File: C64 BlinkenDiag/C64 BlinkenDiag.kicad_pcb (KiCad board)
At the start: 2 copper layers, 99.4 x 99.9 mm, 13 parts, among them J1 C64-Exp-Port, J2 Voltmeter, M1 Mounting, M2 Mounting, M3 Mounting, M4 Mounting, SW1 ROM_EN, SW2 Function, SW3 Bank, SW4 Reset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

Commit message: Did a layout
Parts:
- added A1: module, voltmeter:voltage_display_036, F.Cu at (191.4, 28.6)
- added C1: 100nF, Capacitor_THT:C_Disc_D4.7mm_W2.5mm_P5.00mm, F.Cu at (135.5, 87.0)
- added C2: 100nF, Capacitor_THT:C_Disc_D4.7mm_W2.5mm_P5.00mm, F.Cu at (132.3, 37.5)
- added C3: 100nF, Capacitor_THT:C_Disc_D4.7mm_W2.5mm_P5.00mm, F.Cu at (146.3, 37.5)
- added C4: 100nF, Capacitor_THT:C_Disc_D4.7mm_W2.5mm_P5.00mm, F.Cu at (169.8, 74.3)
- added C5: 100nF, Capacitor_THT:C_Disc_D4.7mm_W2.5mm_P5.00mm, F.Cu at (138.0, 74.3)
- added C6: 10uF, Capacitor_THT:CP_Radial_D4.0mm_P2.00mm, F.Cu at (124.1, 82.5)
- added D1: RESET, LED_THT:LED_D5.0mm, F.Cu at (169.2, 26.0)
- added D10: D6, LED_THT:LED_D5.0mm, F.Cu at (161.5, 41.3)
- added D11: D5, LED_THT:LED_D5.0mm, F.Cu at (168.5, 41.3)
- added D12: D4, LED_THT:LED_D5.0mm, F.Cu at (175.5, 41.3)
- added D13: D3, LED_THT:LED_D5.0mm, F.Cu at (183.1, 41.3)
- added D14: D2, LED_THT:LED_D5.0mm, F.Cu at (190.1, 41.3)
- added D15: D1, LED_THT:LED_D5.0mm, F.Cu at (197.1, 41.3)
- added D16: D0, LED_THT:LED_D5.0mm, F.Cu at (204.1, 41.3)
- added D17: A15, LED_THT:LED_D5.0mm, F.Cu at (154.6, 52.7)
- added D18: A14, LED_THT:LED_D5.0mm, F.Cu at (161.5, 52.7)
- added D19: A13, LED_THT:LED_D5.0mm, F.Cu at (168.5, 52.7)
- added D2: GAME, LED_THT:LED_D5.0mm, F.Cu at (131.7, 26.0)
- added D20: A12, LED_THT:LED_D5.0mm, F.Cu at (175.5, 52.7)
- added D21: A11, LED_THT:LED_D5.0mm, F.Cu at (183.1, 52.7)
- added D22: A10, LED_THT:LED_D5.0mm, F.Cu at (190.1, 52.7)
- added D23: A9, LED_THT:LED_D5.0mm, F.Cu at (197.1, 52.7)
- added D24: A8, LED_THT:LED_D5.0mm, F.Cu at (204.1, 52.7)
- added D25: A7, LED_THT:LED_D5.0mm, F.Cu at (154.6, 64.1)
- added D26: A6, LED_THT:LED_D5.0mm, F.Cu at (161.5, 64.1)
- added D27: A5, LED_THT:LED_D5.0mm, F.Cu at (168.5, 64.1)
- added D28: A4, LED_THT:LED_D5.0mm, F.Cu at (175.5, 64.1)
- added D29: A3, LED_THT:LED_D5.0mm, F.Cu at (183.1, 64.1)
- added D3: EXROM, LED_THT:LED_D5.0mm, F.Cu at (138.7, 26.0)
- added D30: A2, LED_THT:LED_D5.0mm, F.Cu at (190.1, 64.1)
- added D31: A1, LED_THT:LED_D5.0mm, F.Cu at (197.1, 64.1)
- added D32: A0, LED_THT:LED_D5.0mm, F.Cu at (204.1, 64.1)
- added D4: IO2, LED_THT:LED_D5.0mm, F.Cu at (145.7, 26.0)
- added D5: IO1, LED_THT:LED_D5.0mm, F.Cu at (152.7, 26.0)
- added D6: WRITE, LED_THT:LED_D5.0mm, F.Cu at (162.2, 26.0)
- added D7: IRQ, LED_THT:LED_D5.0mm, F.Cu at (162.2, 33.0)
- added D8: NMI, LED_THT:LED_D5.0mm, F.Cu at (169.2, 33.0)
- added D9: D7, LED_THT:LED_D5.0mm, F.Cu at (154.6, 41.3)
- added JP1: EN_SIGNAL, Connector_PinHeader_2.54mm:PinHeader_1x03_P2.54mm_Vertical, F.Cu at (124.7, 70.5)
- added JP2: EN_DATA, Connector_PinHeader_2.54mm:PinHeader_1x03_P2.54mm_Vertical, F.Cu at (127.3, 70.5)
- added JP3: EN_ADDR, Connector_PinHeader_2.54mm:PinHeader_1x03_P2.54mm_Vertical, F.Cu at (132.3, 70.5)
- added JP4: EN_ADDR, Connector_PinHeader_2.54mm:PinHeader_1x03_P2.54mm_Vertical, F.Cu at (134.9, 70.5)
- added RN1: 330x8, Resistor_THT:R_Array_SIP9, F.Cu at (157.1, 45.7)
- added RN2: 330x8, Resistor_THT:R_Array_SIP9, F.Cu at (131.7, 32.4)
- added RN3: 330x8, Resistor_THT:R_Array_SIP9, F.Cu at (157.1, 57.1)
- added RN4: 330x8, Resistor_THT:R_Array_SIP9, F.Cu at (157.1, 68.6)
- added U2: 74HCT540, Package_DIP:DIP-20_W7.62mm_Socket_LongPads, F.Cu at (124.7, 41.3)
- added U3: 74HCT573, Package_DIP:DIP-20_W7.62mm_Socket_LongPads, F.Cu at (138.7, 41.3)
- added U4: 74HCT573, Package_DIP:DIP-20_W7.62mm_Socket_LongPads, F.Cu at (173.6, 81.9)
- added U5: 74HCT573, Package_DIP:DIP-20_W7.62mm_Socket_LongPads, F.Cu at (141.9, 81.9)
- M1, M2, M3, M4: footprint mounting:M3 -> mounting:M3_pin
- SW2: value Function -> FUNCTION
- SW3: value Bank -> ROM_BANK
- SW4: value Reset -> RESET
- moved SW2 213.0 mm to (214.2, 54.0)
- moved J2 204.2 mm to (215.5, 33.0), turned to 180 degrees
- moved SW1 202.6 mm to (214.2, 76.8)
- moved SW3 198.0 mm to (214.2, 65.4)
- moved R2 121.0 mm to (125.1, 99.1)
- moved R1 113.0 mm to (125.1, 95.9)
- moved SW4 36.6 mm to (214.2, 41.9)
- moved U1 2.29 mm to (139.3, 102.2)
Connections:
- net A13 renamed ROM_A13
- net A14 renamed ROM_A14
- net ~ROM renamed ~ROM_CS
- J1 pad 10: (no net) -> /~IO2
- J1 pad 4: (no net) -> /~IRQ
- J1 pad 5: (no net) -> /R~W
- J1 pad 7: (no net) -> /~IO1
- J1 pad D: (no net) -> /~NMI
- J1 pad E: (no net) -> /PHI2
- J1 pad F: Net-(J1-PadF) -> /A15
- J1 pad H: Net-(J1-PadH) -> /A14
- J1 pad J: Net-(J1-PadJ) -> /A13
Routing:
- net VCC: track 0.00 -> 273.5 mm, vias 0 -> 4
- net ~RESET: track 0.00 -> 212.4 mm, vias 0 -> 1
- net ~GAME: track 0.00 -> 171.6 mm, vias 0 -> 8
- net ~EXROM: track 0.00 -> 161.5 mm, vias 0 -> 4
- net ~ROMH: track 0.00 -> 146.5 mm, vias 0 -> 7
- net /PHI2: track 0.00 -> 135.9 mm, vias 0 -> 3
- net ROM_A13: track 0.00 -> 130.9 mm, vias 0 -> 3
- net ~ROML: track 0.00 -> 128.5 mm, vias 0 -> 4
- net Net-(D18-Pad2): track 0.00 -> 110.3 mm
- net /D6: track 0.00 -> 98.2 mm, vias 0 -> 1
- net Net-(D19-Pad2): track 0.00 -> 97.8 mm
- net ~ROM_CS: track 8.15 -> 105.6 mm, vias 0 -> 2
- net Net-(D17-Pad2): track 0.00 -> 97.0 mm, vias 0 -> 2
- net ROM_A14: track 0.00 -> 96.1 mm, vias 0 -> 4
- net /D7: track 0.00 -> 95.1 mm, vias 0 -> 1
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- added copper zone on F.Cu, net VCC
- removed copper zone on F.Cu, net +5V

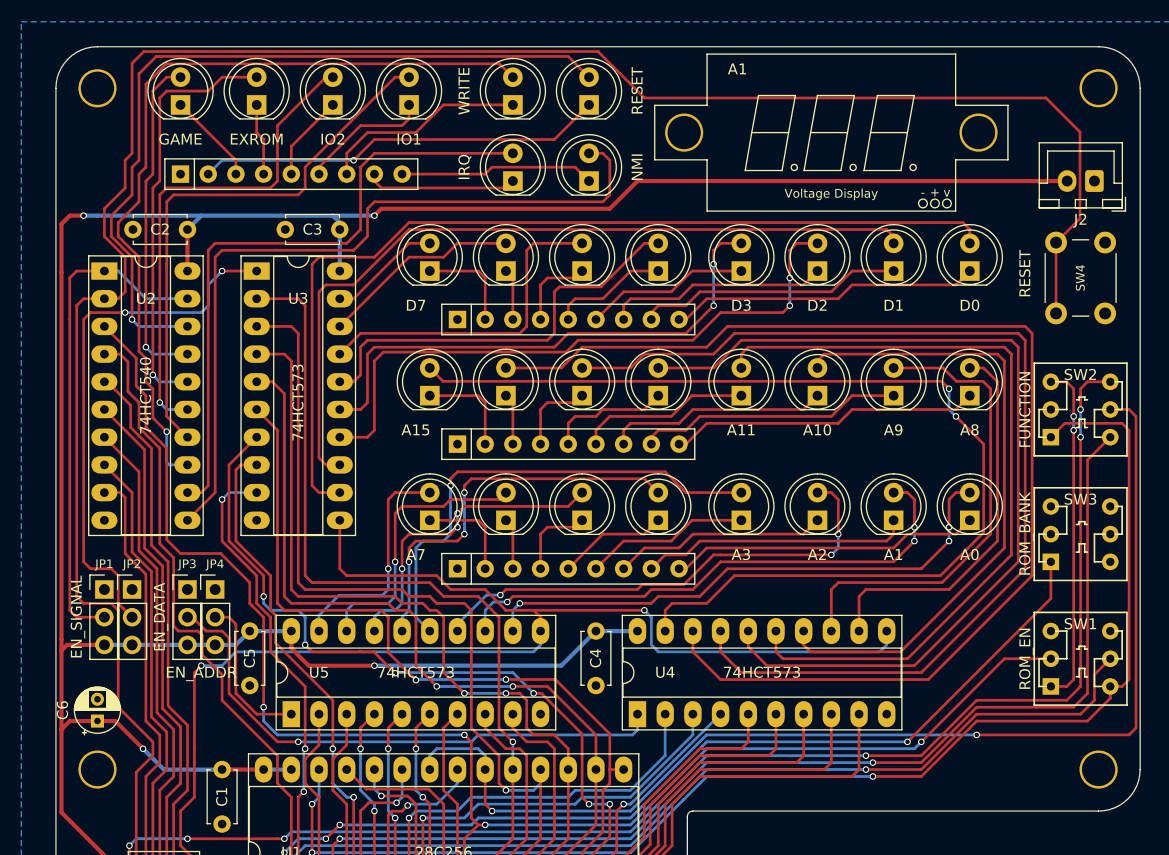
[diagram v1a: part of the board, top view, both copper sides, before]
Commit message: Tweaked silkscreen and gerber export
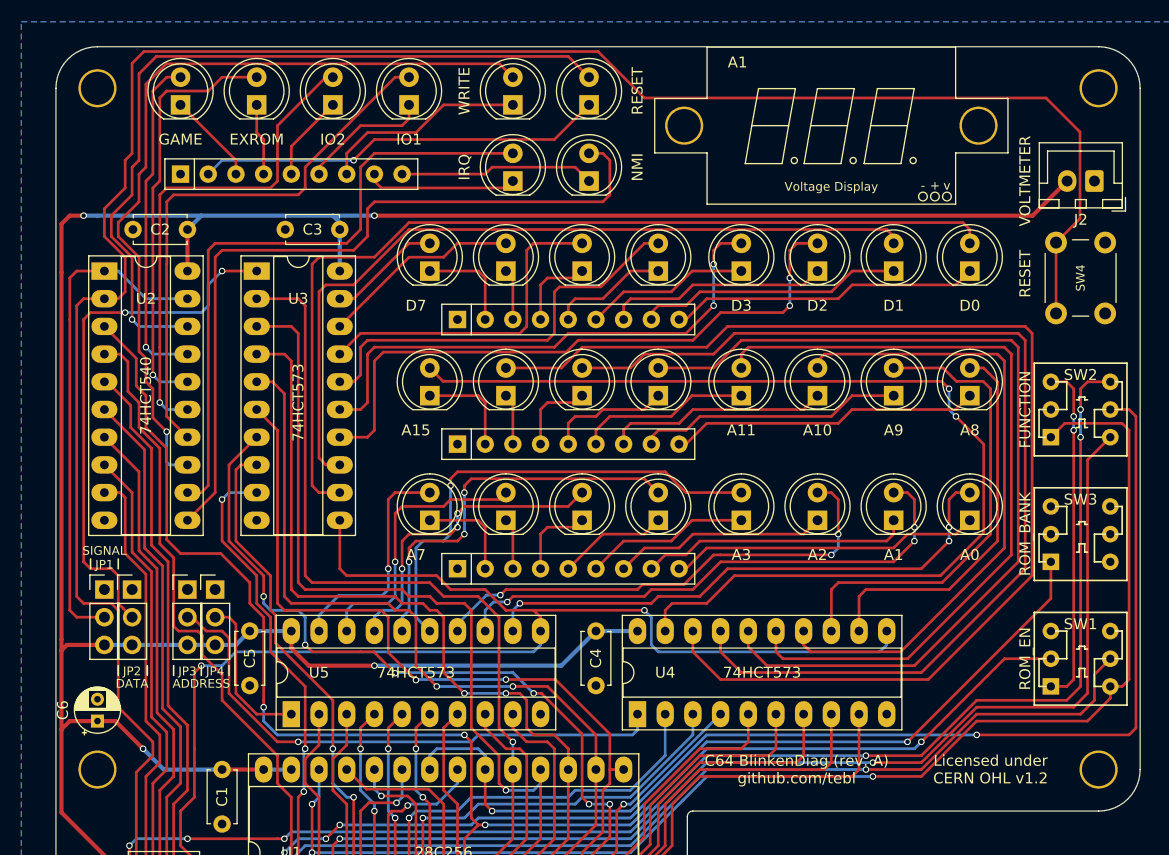
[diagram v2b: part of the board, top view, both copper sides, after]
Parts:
- J2: value Voltmeter -> VOLTMETER
- moved A1 0.63 mm to (191.4, 27.9)
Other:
- board text added: "ADDRESS"
- board text added: "C64 BlinkenDiag (rev. A) github.com/tebl"
- board text added: "DATA"
- board text added: "GND"
- board text added: "LED Output: 1-2 Enabled 2-3 Disabled"
- board text added: "Licensed under CERN OHL v1.2"
- board text added: "SIGNAL"
- board text added: "VCC"

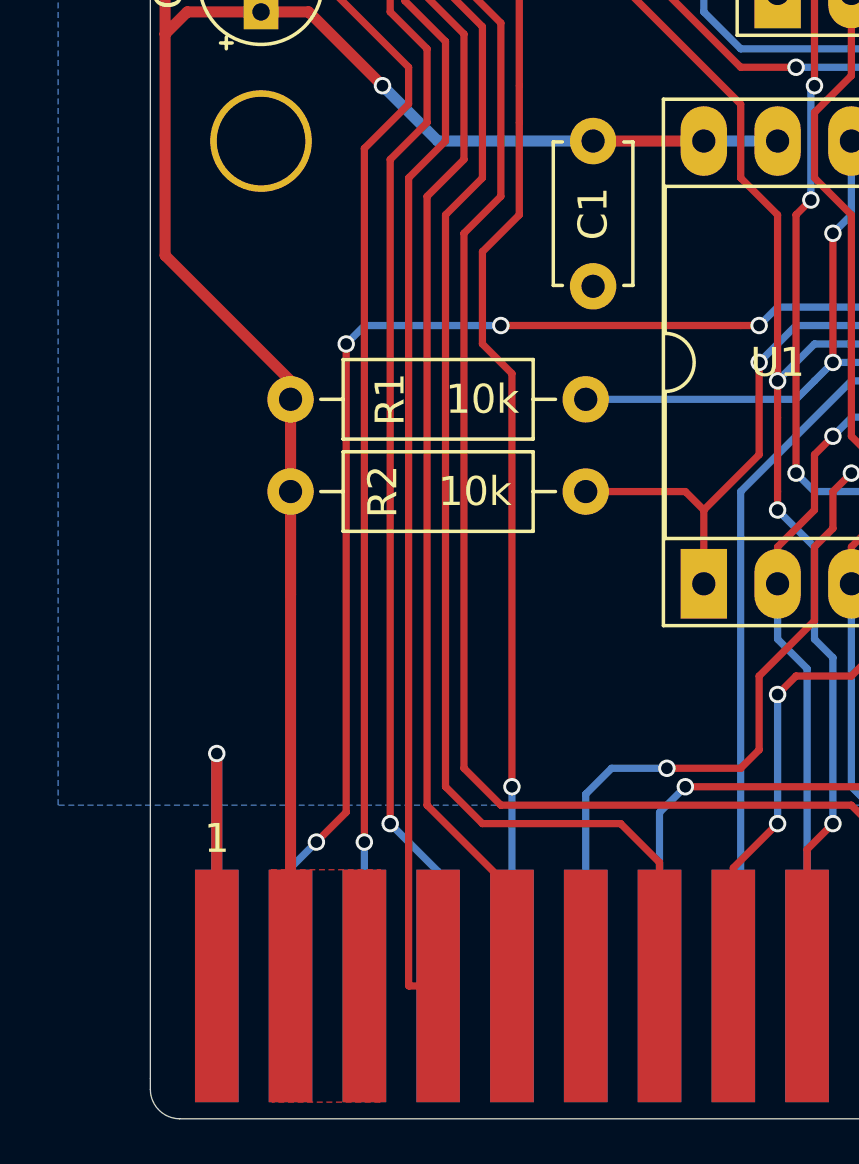
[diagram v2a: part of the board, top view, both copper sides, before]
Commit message: Add PCB preview
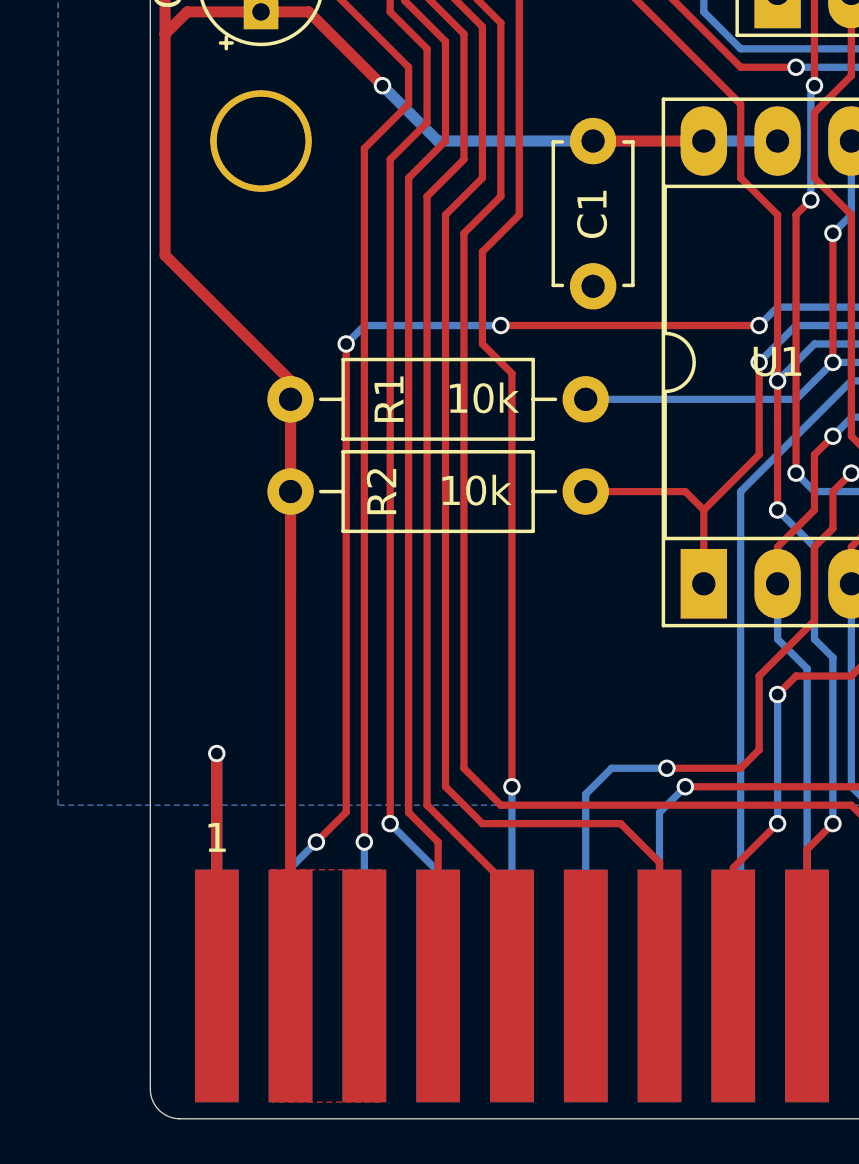
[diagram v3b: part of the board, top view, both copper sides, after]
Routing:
- net /~IRQ: track 60.9 -> 60.3 mm

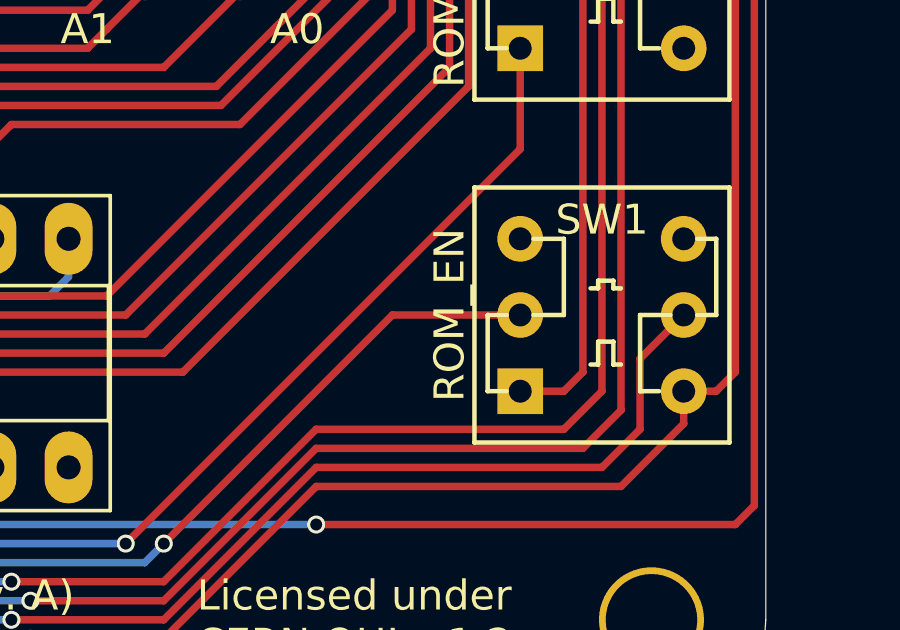
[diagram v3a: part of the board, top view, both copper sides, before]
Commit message: Added faceplate and changed ROM_EN to ROM_DIS
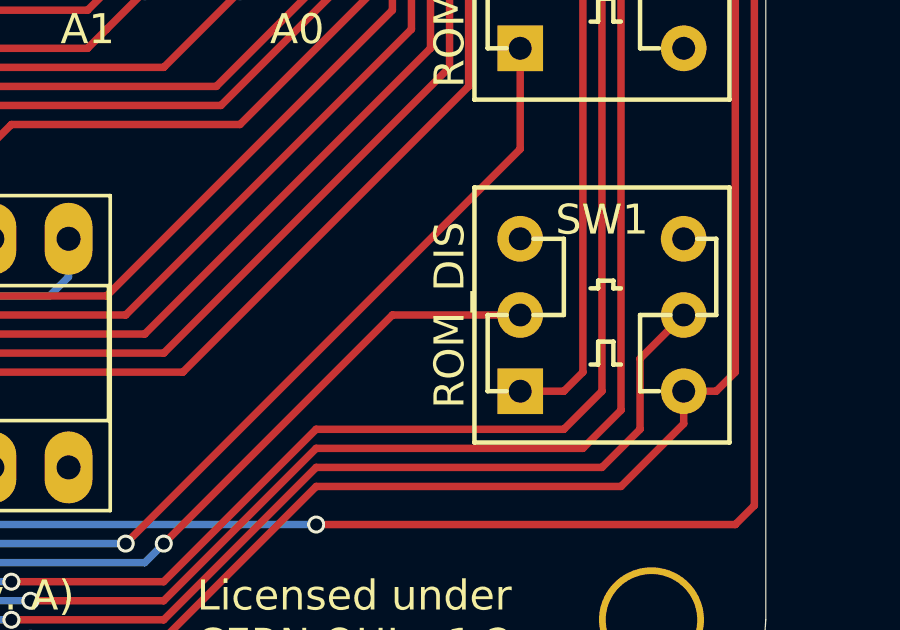
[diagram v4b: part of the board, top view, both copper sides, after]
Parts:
- SW1: value ROM_EN -> ROM_DIS
